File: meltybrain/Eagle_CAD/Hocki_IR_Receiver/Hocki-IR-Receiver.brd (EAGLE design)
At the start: 42 x 35 mm, 74 parts, among them J1 SM03B-SRSS-TB(LF)(SN), U1 OPA2380AIDGKR, U10 NL27WZ32USG, U11 TMUX1204DGSR, U2 OPA2380AIDGKR, U3 AP2210K-5.0TRG1, U4 LMH6612MAX/NOPB, U5 LMH6612MAX/NOPB, U6 TLV73310PDBVT, U7 TLV3502AIDCNR, U8 TLV3502AIDCNR, U9 SN74LVC1G58DCKR

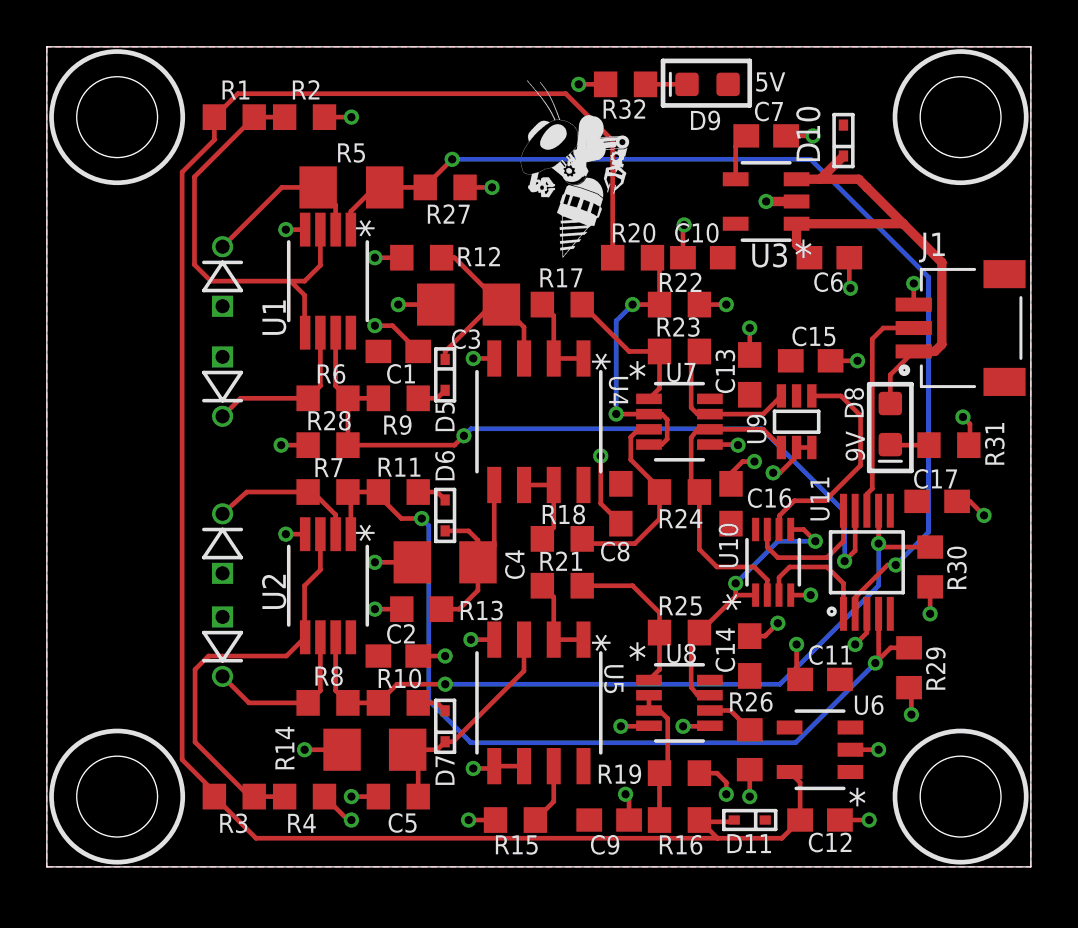
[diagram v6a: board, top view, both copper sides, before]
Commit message: receiver now 4 layers
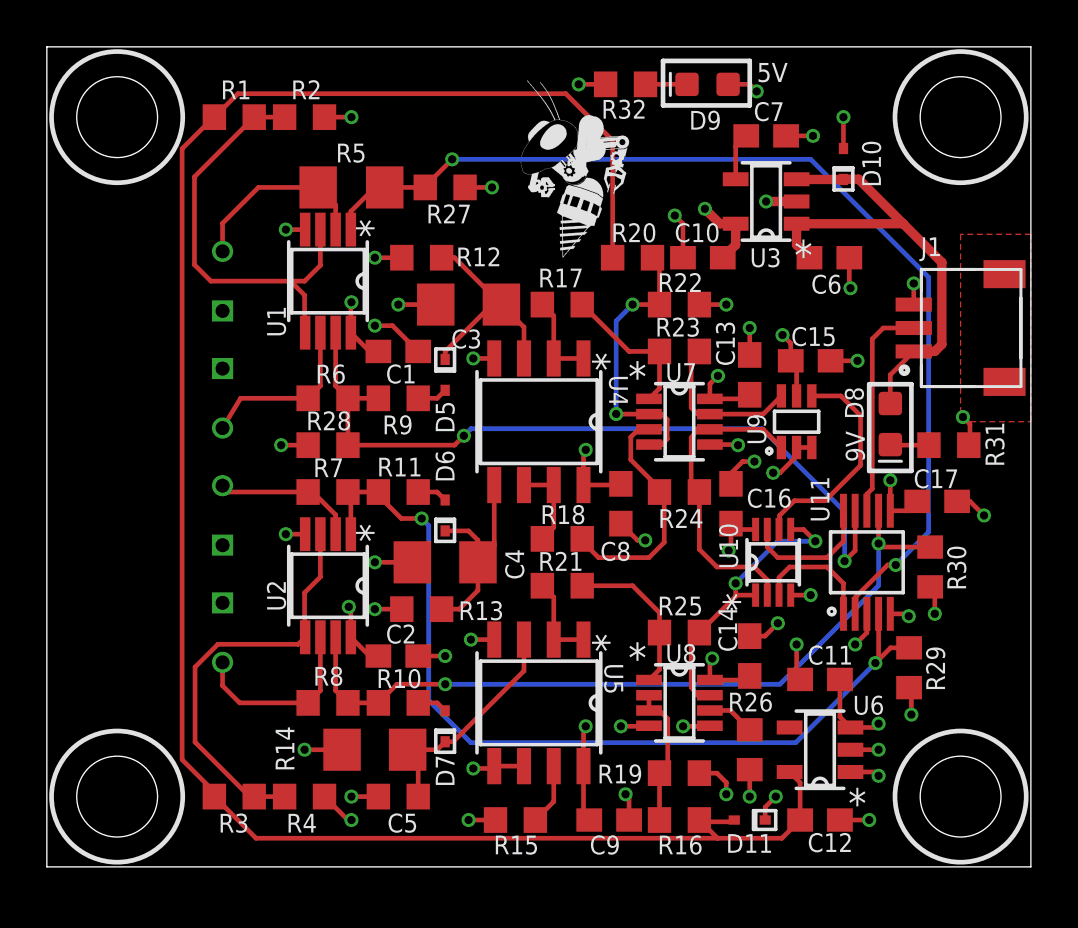
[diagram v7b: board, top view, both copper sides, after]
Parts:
- moved D2 1.20 mm to (7.50, 15.0)
- moved D10 1.00 mm to (34.0, 30.0)
- moved D4 0.60 mm to (7.50, 10.0)
- moved D3 0.50 mm to (7.50, 20.0)
- moved D1 0.20 mm to (7.50, 25.0)
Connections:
- net 5V: no longer J1.S1, J1.S2
- net GND: now also J1.S1, J1.S2
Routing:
- net 5V: track 0.00 -> 39.1 mm, vias 0 -> 16
- net N$20: track 8.74 -> 10.2 mm
- net 9V: track 22.8 -> 21.4 mm
- net GND: track 62.1 -> 60.8 mm
- net N$10: track 7.14 -> 7.97 mm
- net N$1: track 7.24 -> 8.02 mm
- added copper zone on layer 15, net 5V
- added copper zone on layer 1, net GND
- added copper zone on layer 2, net GND
- removed copper zone on layer 1, net 5V
- removed copper zone on layer 16, net GND

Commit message: tvs diodes and removed 1v regulator
1v supplied with free opamp
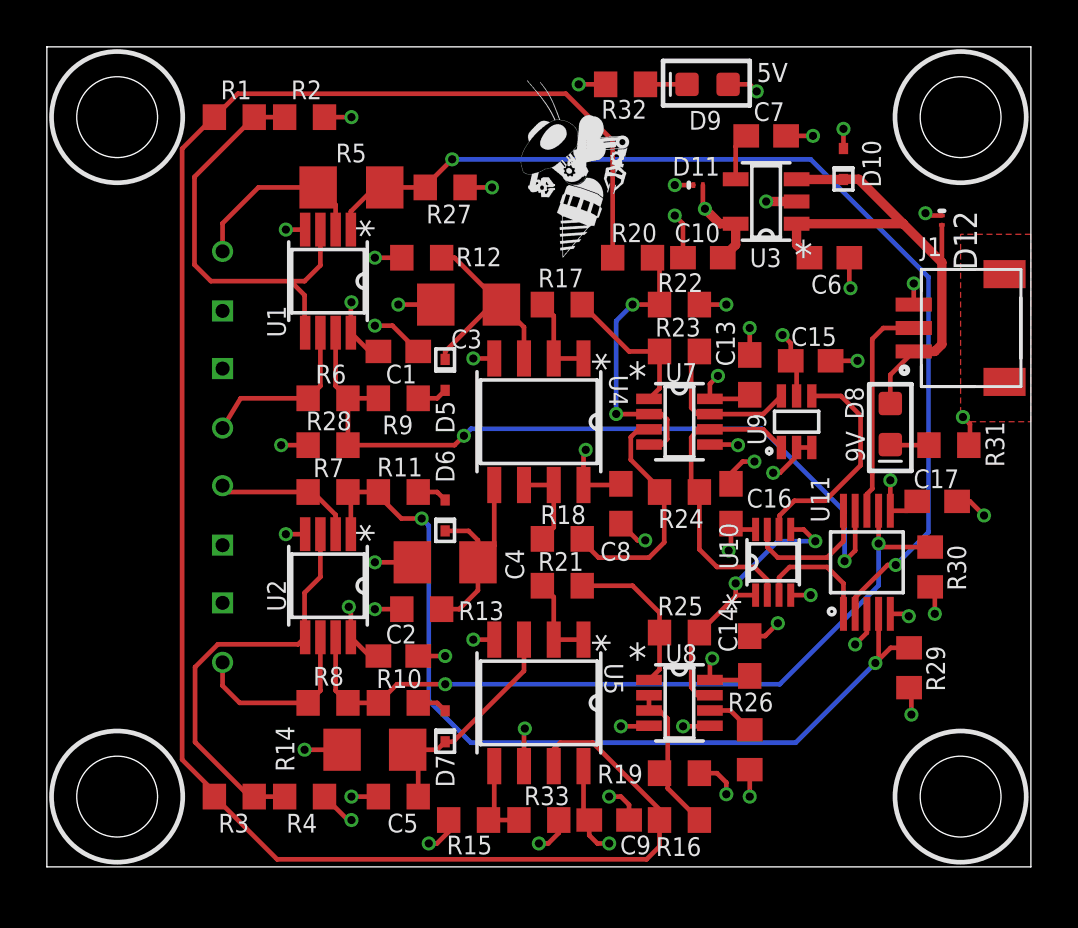
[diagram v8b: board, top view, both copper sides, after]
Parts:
- removed C11, C12: 1uF, rcl:C0603
- removed U6: TLV73310PDBVT, Hocki_Library:SOT-23-5
- added D12: ESDZX051-1BF4, Hocki_Library:DSN0603-2
- added R33: 97.6, resistor:R0603
- D11: value BAS581-02V-V-G-08 -> PESD5V0H1BSFYL; device Hocki_Library:SOD-523 -> Hocki_Library:DSN0603-2
- R15: value 499 -> 392
- moved D11 27.2 mm to (27.8, 29.1), turned to 0 degrees
- moved R15 2.00 mm to (18.0, 2.00)
- turned R16 to 180 degrees
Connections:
- removed net N$19: R15.2, U5.7
- new net N$15: R15.2, R33.1, U5.5
- net 1.0V: now also U5.7; no longer C12.1, D11.2, U6.5
- net 5V: now also D11.C2, R15.1; no longer C11.1, D11.1, U6.1, U6.3
- net 9V: now also D12.C2
- net GND: now also D11.C1, D12.C1, R33.2; no longer C11.2, C12.2, R15.1, U5.5, U6.2
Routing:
- net 5V: track 39.1 -> 35.2 mm, vias 16 -> 14
- net N$15: track 0.00 -> 3.70 mm
- net N$19: track 2.63 -> 0.00 mm
- net 1.0V: track 84.2 -> 81.9 mm
- net GND: track 60.8 -> 58.6 mm, vias 46 -> 45
- net 9V: track 21.4 -> 23.0 mm
- net N$14: track 6.06 -> 6.97 mm
